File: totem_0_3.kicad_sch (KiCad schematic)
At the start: 44 parts, among them J1 MJ-4PP-9, J2 MJ-4PP-9, U3 RP2040, U4 RP2040

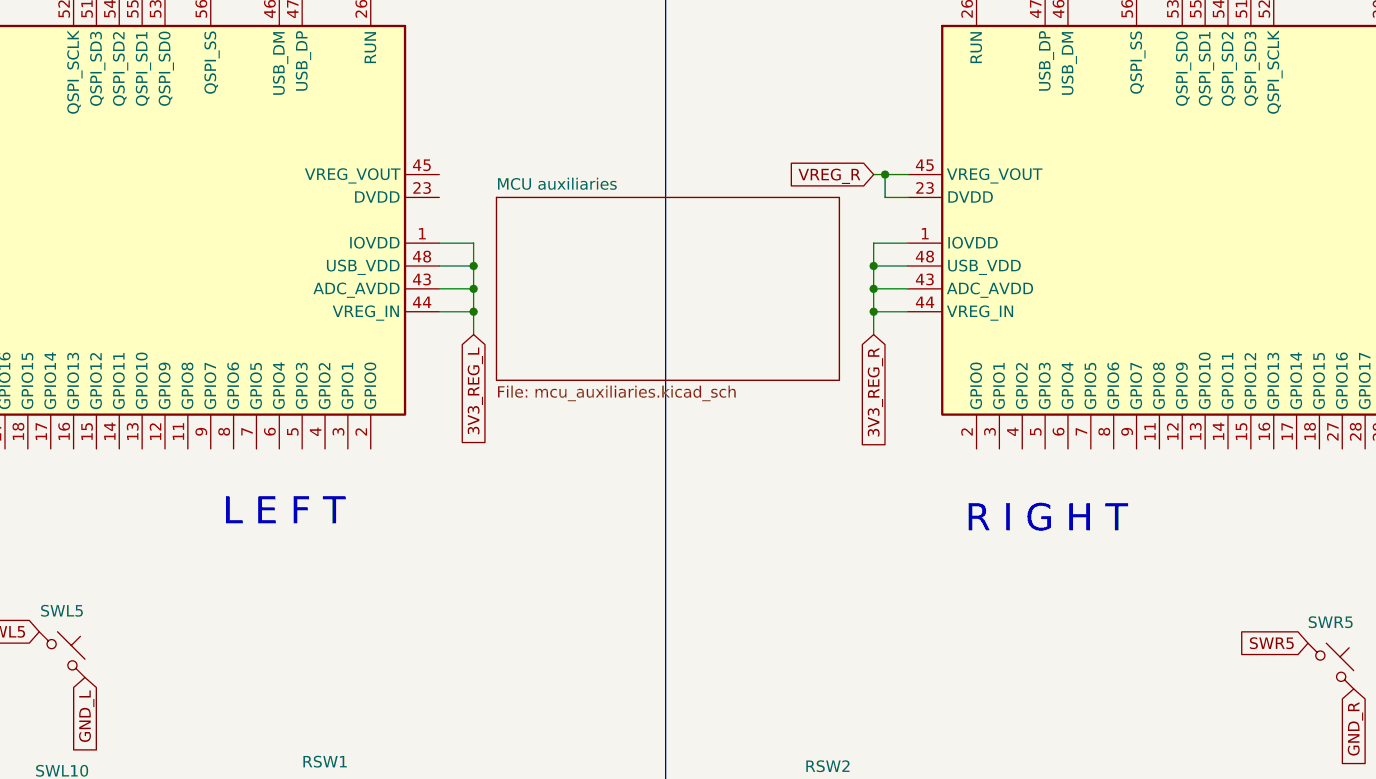
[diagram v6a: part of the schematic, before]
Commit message: Fix left mcu vreg
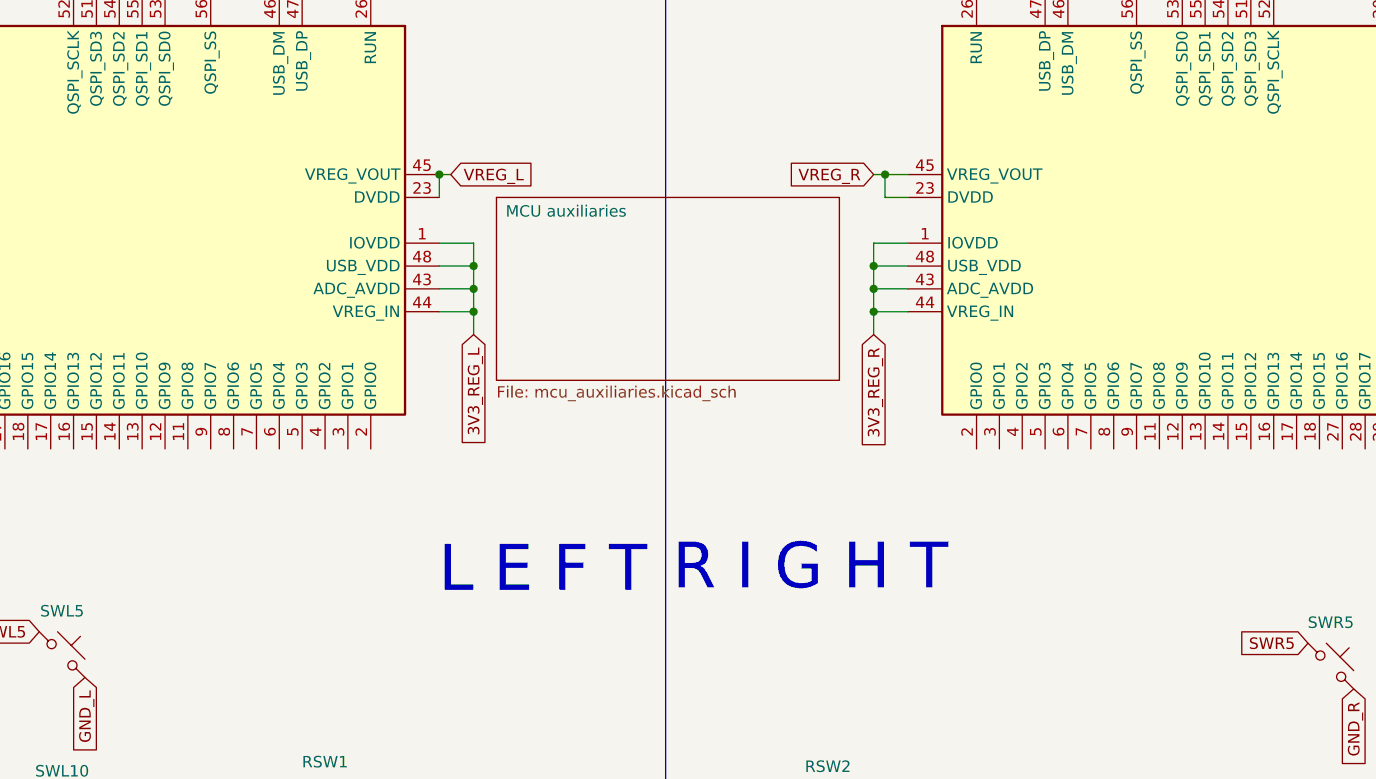
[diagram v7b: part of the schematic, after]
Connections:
- net VREG_L: now reaches U3.23 (DVDD), U3.50 (DVDD)
- net VREG_L: now also U3.45 (VREG_VOUT)
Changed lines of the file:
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@@
 	)
 	(junction
+		(at 123.19 43.18)
+		(diameter 0)
+		(color 0 0 0 0)
+	)
+	(junction
 		(at 127 55.88)
 		(diameter 0)
@@
 	(wire
 		(pts
+			(xy 123.19 43.18) (xy 124.46 43.18)
+		)
+		(stroke
+			(width 0)
+			(type default)
+		)
+	)
+	(wire
+		(pts
 			(xy 171.45 55.88) (xy 175.26 55.88)
 		)
@@
 	(wire
 		(pts
+			(xy 123.19 43.18) (xy 123.19 45.72)
+		)
+		(stroke
+			(width 0)
+			(type default)
+		)
+	)
+	(wire
+		(pts
 			(xy 127 55.88) (xy 123.19 55.88)
 		)
@@
 	(text "R I G H T"
 		(exclude_from_sim no)
-		(at 181.61 83.312 0)
+		(at 149.098 89.916 0)
 		(effects
 			(font
-				(size 3 3)
+				(size 5.08 5.08)
 			)
 			(justify left bottom)
@@
 	(text "L E F T"
 		(exclude_from_sim no)
-		(at 112.776 82.55 0)
+		(at 146.304 90.17 0)
 		(effects
 			(font
-				(size 3 3)
+				(size 5.08 5.08)
 			)
 			(justify right bottom)
@@
 		)
 	)
+	(global_label "VREG_L"
+		(shape input)
+		(at 124.46 43.18 0)
+		(fields_autoplaced yes)
+		(effects
+			(font
+				(size 1.27 1.27)
+			)
+			(justify left)
+		)
+		(property "Intersheetrefs" "${INTERSHEET_REFS}"
+			(at 134.2185 43.18 0)
+			(effects
+				(font
+					(size 1.27 1.27)
+				)
+				(justify left)
+				(hide yes)
+			)
+		)
+	)
 	(global_label "GND_L"
 		(shape input)
@@
 		(at 129.54 45.72)
 		(size 38.1 20.32)
-		(fields_autoplaced yes)
 		(stroke
 			(width 0.1524)
@@
 		)
 		(property "Sheetname" "MCU auxiliaries"
-			(at 129.54 45.0084 0)
+			(at 130.556 48.006 0)
 			(effects
 				(font

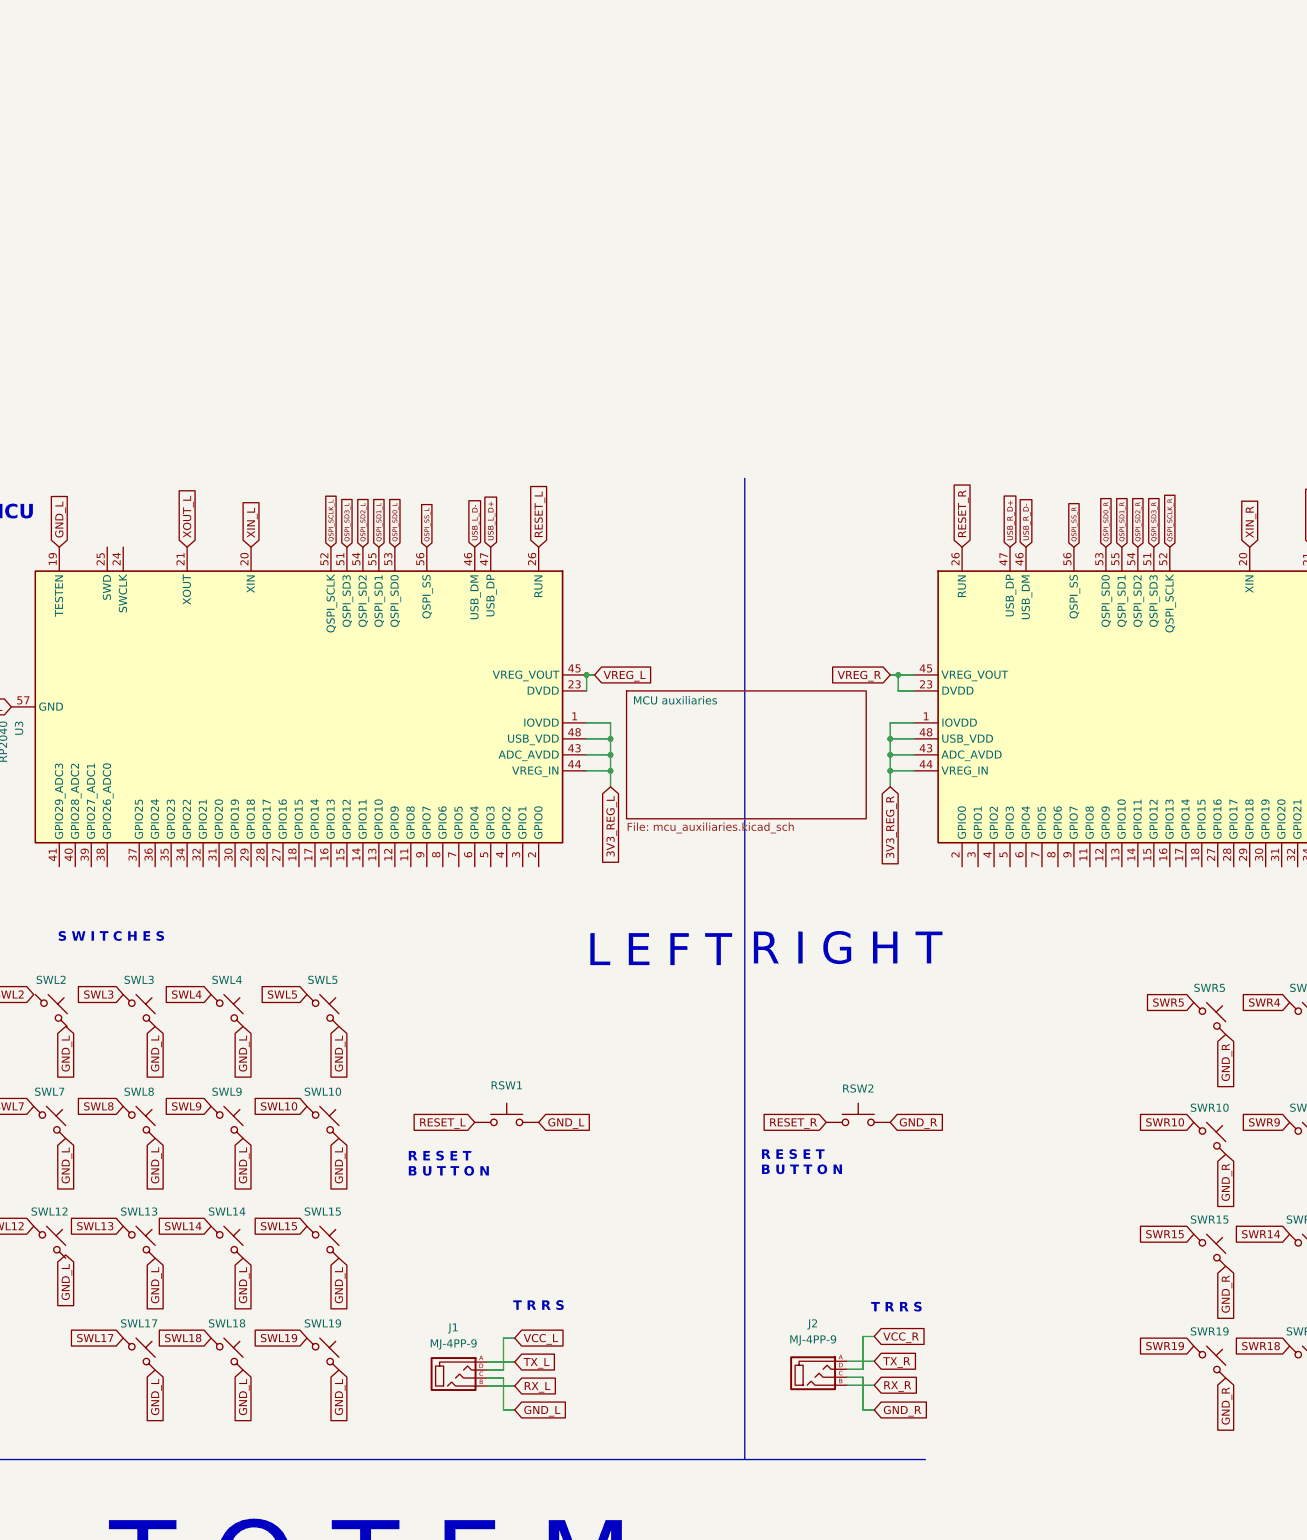
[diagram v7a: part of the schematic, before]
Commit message: Add usb-c ss connector
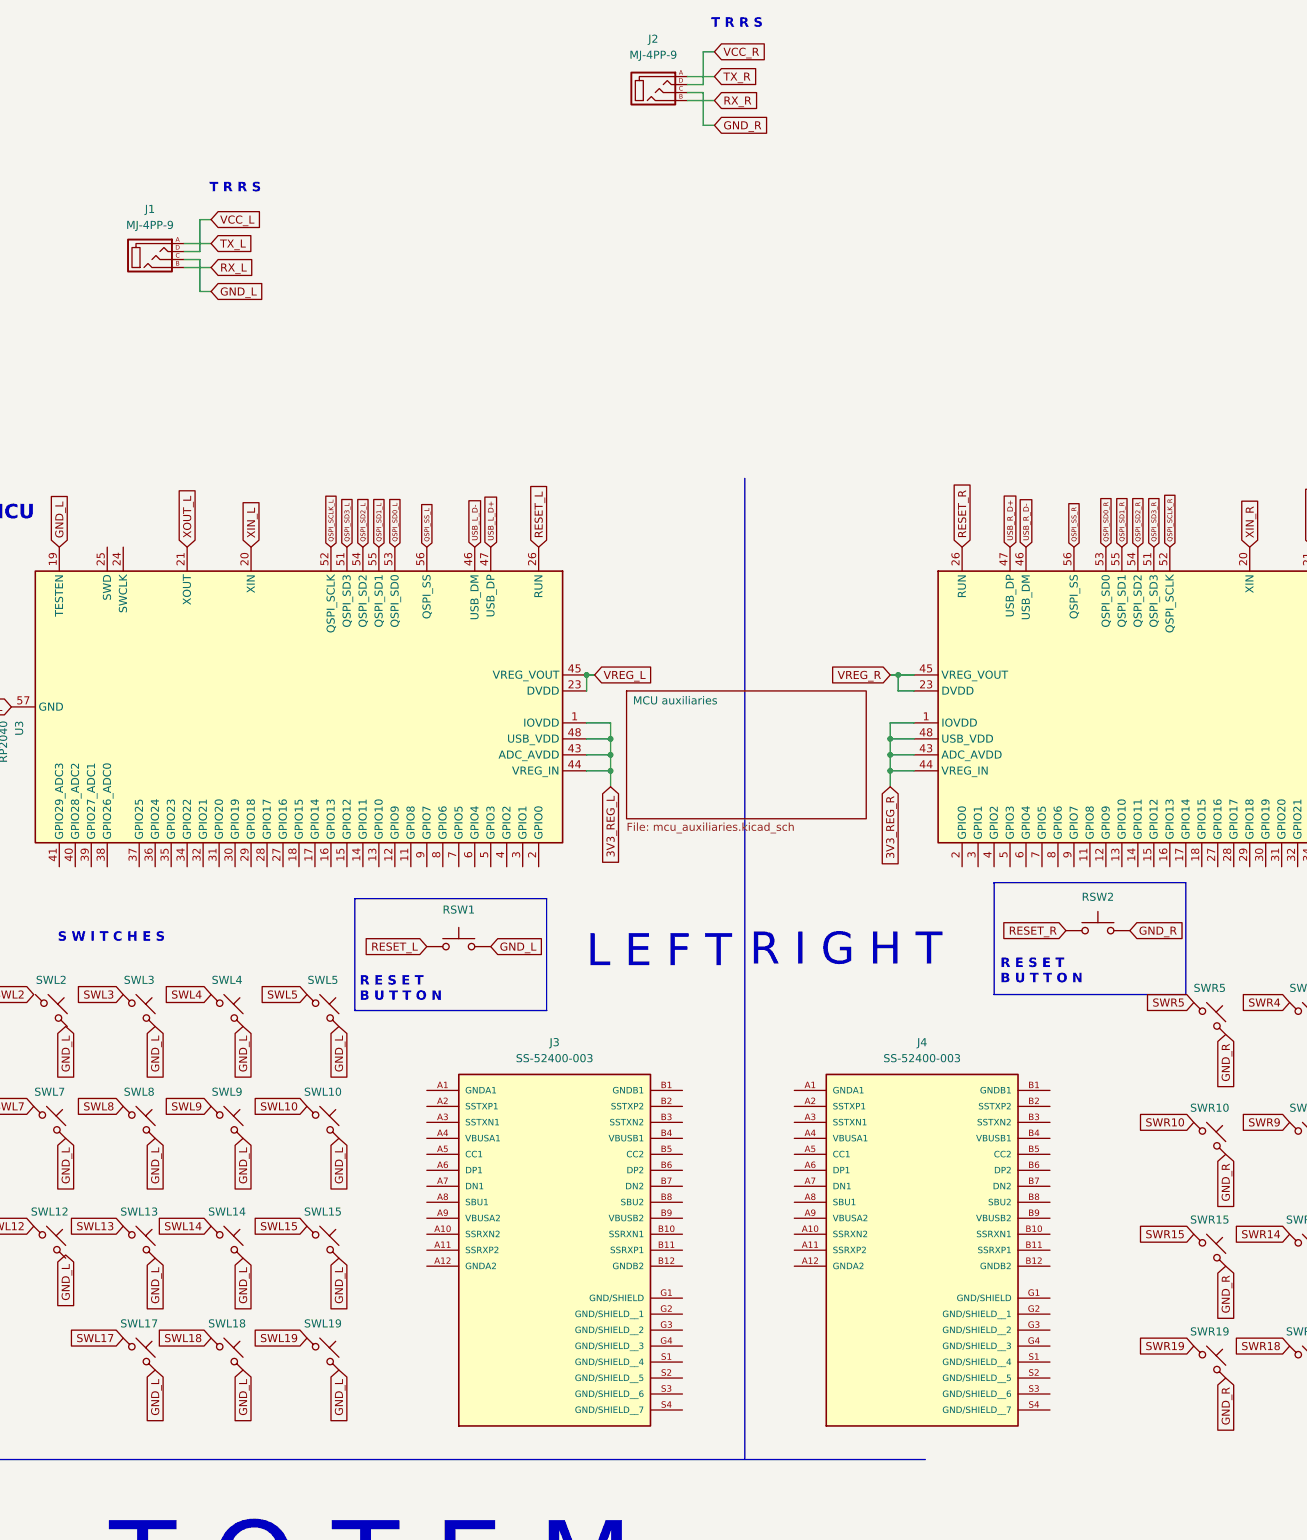
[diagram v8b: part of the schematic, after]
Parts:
- added J3, J4: SS-52400-003, SS-52400-003:BELFUSE_SS-52400-003, symbol USB-C-SS:SS-52400-003
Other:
- moved on the sheet: J1, J2, RSW1, RSW2
